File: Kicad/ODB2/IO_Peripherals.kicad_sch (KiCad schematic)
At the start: 22 parts, among them J5 RFM_Conn_Coaxial, U10 W25Q512JVEIQ

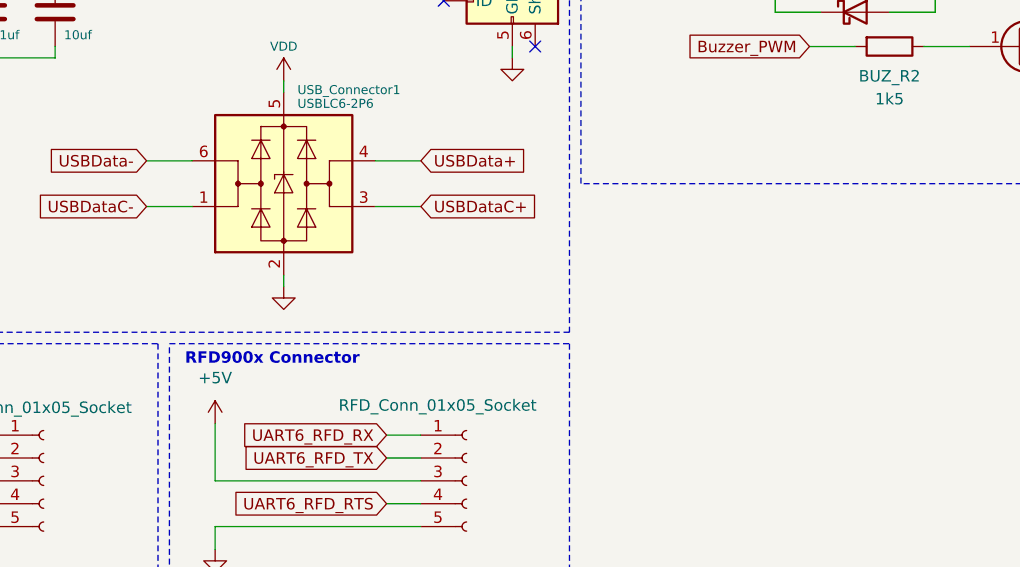
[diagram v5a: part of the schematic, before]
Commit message: ajout IO_Camera + stm32cubeide
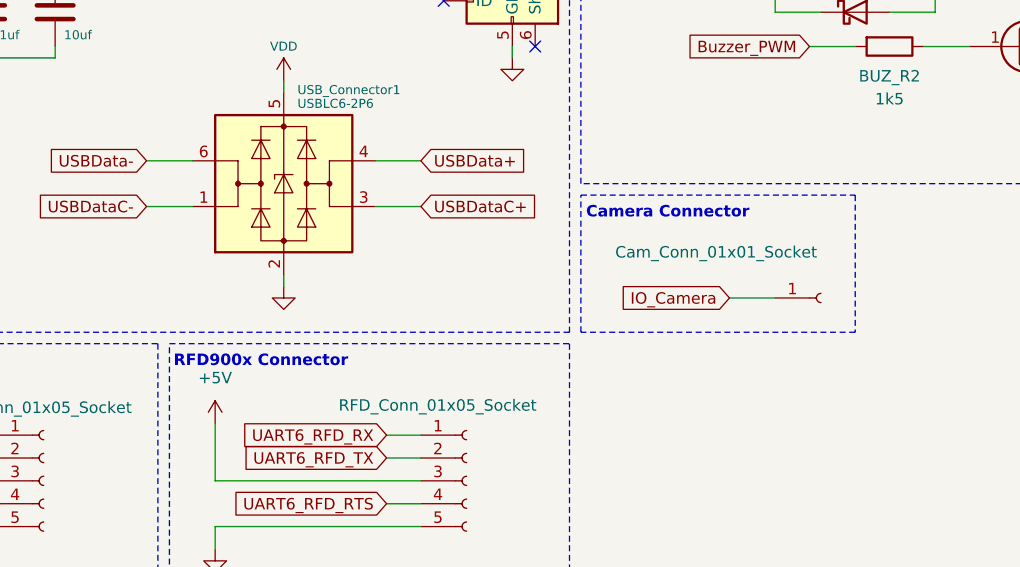
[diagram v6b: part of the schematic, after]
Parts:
- added J1: Cam_Conn_01x01_Socket, Connector_PinHeader_2.00mm:PinHeader_1x01_P2.00mm_Vertical, symbol Connector:Conn_01x01_Socket
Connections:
- new net IO_Camera: J1.1 (Pin_1)
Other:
- note added: "Camera Connector"
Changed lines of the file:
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@@
+	(wire
+		(pts
+			(xy 121.92 74.93) (xy 127 74.93)
+		)
+		(stroke
+			(width 0)
+			(type default)
+		)
+	)
 	(wire
 		(pts
@@
 			(width 0)
 			(type default)
+		)
+	)
+	(rectangle
+		(start 105.41 63.5)
+		(end 135.89 78.74)
+		(stroke
+			(width 0)
+			(type dash)
+		)
+		(fill
+			(type none)
 		)
 	)
@@
 		)
 	)
+	(text "Camera Connector"
+		(exclude_from_sim no)
+		(at 115.062 65.532 0)
+		(effects
+			(font
+				(size 1.27 1.27)
+				(thickness 0.254)
+				(bold yes)
+			)
+		)
+	)
 	(text "Standard SPI D0"
 		(exclude_from_sim no)
@@
 	(text "RFD900x Connector"
 		(exclude_from_sim no)
-		(at 71.12 81.788 0)
+		(at 69.85 82.042 0)
 		(effects
 			(font
@@
 		(property "Intersheetrefs" "${INTERSHEET_REFS}"
 			(at 116.3344 46.99 0)
+			(effects
+				(font
+					(size 1.27 1.27)
+				)
+				(justify right)
+				(hide yes)
+			)
+		)
+	)
+	(global_label "IO_Camera"
+		(shape input)
+		(at 121.92 74.93 180)
+		(fields_autoplaced yes)
+		(effects
+			(font
+				(size 1.27 1.27)
+			)
+			(justify right)
+		)
+		(property "Intersheetrefs" "${INTERSHEET_REFS}"
+			(at 108.8958 74.93 0)
 			(effects
 				(font
@@
 					(unit 1)
 				)
+			)
+		)
+	)
+	(symbol
+		(lib_id "Connector:Conn_01x01_Socket")
+		(at 132.08 74.93 0)
+		(unit 1)
+		(exclude_from_sim no)
+		(in_bom yes)
+		(on_board yes)
+		(dnp no)
+		(property "Reference" "J1"
+			(at 133.35 73.6599 0)
+			(effects
+				(font
+					(size 1.27 1.27)
+				)
+				(justify left)
+				(hide yes)
+			)
+		)
+		(property "Value" "Cam_Conn_01x01_Socket"
+			(at 109.22 69.85 0)
+			(effects
+				(font
+					(size 1.27 1.27)
+				)
+				(justify left)
+			)
+		)
+		(property "Footprint" "Connector_PinHeader_2.00mm:PinHeader_1x01_P2.00mm_Vertical"
+			(at 132.08 74.93 0)
+			(effects
+				(font
+					(size 1.27 1.27)
+				)
+				(hide yes)
+			)
+		)
+		(property "Datasheet" "~"
+			(at 132.08 74.93 0)
+			(effects
+				(font
+					(size 1.27 1.27)
+				)
+				(hide yes)
+			)
+		)
+		(property "Description" "Generic connector, single row, 01x01, script generated"
+			(at 132.08 74.93 0)
+			(effects
+				(font
+					(size 1.27 1.27)
+				)
+				(hide yes)
+			)
+		)
+		(pin "1"
+		)
+		(instances
+			(project ""
+				(path "/4b06c5d1-aa8b-48ed-8972-b43a60cfab78/93865dc8-71fa-4dc6-90ce-f5a9779dfd41"
+					(reference "J1")
+					(unit 1)
+				)

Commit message: fix my shit (cam io)
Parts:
- removed J1: Cam_Conn_01x01_Socket, Connector_PinHeader_2.00mm:PinHeader_1x01_P2.00mm_Vertical, symbol Connector:Conn_01x01_Socket
- added J1: Cam_Conn_01x02_Socket, Connector_PinHeader_2.00mm:PinHeader_1x02_P2.00mm_Vertical, symbol Connector:Conn_01x02_Socket
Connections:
- net GND: now also J1.2 (Pin_2)
- net IO_Camera: now also J1.1 (Pin_1)
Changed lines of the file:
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@@
 	(wire
 		(pts
+			(xy 124.46 76.2) (xy 123.19 76.2)
+		)
+		(stroke
+			(width 0)
+			(type default)
+		)
+	)
+	(wire
+		(pts
 			(xy 54.61 119.38) (xy 54.61 120.65)
 		)
@@
 	(wire
 		(pts
+			(xy 123.19 76.2) (xy 123.19 77.47)
+		)
+		(stroke
+			(width 0)
+			(type default)
+		)
+	)
+	(wire
+		(pts
 			(xy 64.77 95.25) (xy 87.63 95.25)
 		)
@@
 	(wire
 		(pts
-			(xy 121.92 74.93) (xy 127 74.93)
+			(xy 119.38 73.66) (xy 124.46 73.66)
 		)
 		(stroke
@@
 	(rectangle
 		(start 105.41 63.5)
-		(end 135.89 78.74)
+		(end 135.89 83.82)
 		(stroke
 			(width 0)
@@
 	(global_label "IO_Camera"
 		(shape input)
-		(at 121.92 74.93 180)
+		(at 119.38 73.66 180)
 		(fields_autoplaced yes)
 		(effects
@@
 		)
 		(property "Intersheetrefs" "${INTERSHEET_REFS}"
-			(at 108.8958 74.93 0)
+			(at 106.3558 73.66 0)
 			(effects
 				(font
@@
 	)
 	(symbol
-		(lib_id "Connector:Conn_01x01_Socket")
-		(at 132.08 74.93 0)
-		(unit 1)
-		(exclude_from_sim no)
-		(in_bom yes)
-		(on_board yes)
-		(dnp no)
-		(property "Reference" "J1"
-			(at 133.35 73.6599 0)
-			(effects
-				(font
-					(size 1.27 1.27)
-				)
-				(justify left)
-				(hide yes)
-			)
-		)
-		(property "Value" "Cam_Conn_01x01_Socket"
-			(at 109.22 69.85 0)
-			(effects
-				(font
-					(size 1.27 1.27)
-				)
-				(justify left)
-			)
-		)
-		(property "Footprint" "Connector_PinHeader_2.00mm:PinHeader_1x01_P2.00mm_Vertical"
-			(at 132.08 74.93 0)
-			(effects
-				(font
-					(size 1.27 1.27)
-				)
-				(hide yes)
-			)
-		)
-		(property "Datasheet" "~"
-			(at 132.08 74.93 0)
-			(effects
-				(font
-					(size 1.27 1.27)
-				)
-				(hide yes)
-			)
-		)
-		(property "Description" "Generic connector, single row, 01x01, script generated"
-			(at 132.08 74.93 0)
-			(effects
-				(font
-					(size 1.27 1.27)
-				)
-				(hide yes)
-			)
-		)
-		(pin "1"
-		)
-		(instances
-			(project ""
-				(path "/4b06c5d1-aa8b-48ed-8972-b43a60cfab78/93865dc8-71fa-4dc6-90ce-f5a9779dfd41"
-					(reference "J1")
-					(unit 1)
-				)
-			)
-		)
-	)
-	(symbol
 		(lib_id "Device:R")
 		(at 250.19 46.99 90)
@@
 	)
 	(symbol
+		(lib_id "power:GND")
+		(at 123.19 77.47 0)
+		(unit 1)
+		(exclude_from_sim no)
+		(in_bom yes)
+		(on_board yes)
+		(dnp no)
+		(fields_autoplaced yes)
+		(property "Reference" "#PWR082"
+			(at 123.19 83.82 0)
+			(effects
+				(font
+					(size 1 1)
+				)
+				(hide yes)
+			)
+		)
+		(property "Value" "GND"
+			(at 123.19 82.55 0)
+			(effects
+				(font
+					(size 1 1)
+				)
+				(hide yes)
+			)
+		)
+		(property "Footprint" ""
+			(at 123.19 77.47 0)
+			(effects
+				(font
+					(size 1 1)
+				)
+				(hide yes)
+			)
+		)
+		(property "Datasheet" ""
+			(at 123.19 77.47 0)
+			(effects
+				(font
+					(size 1 1)
+				)
+				(hide yes)
+			)
+		)
+		(property "Description" ""
+			(at 123.19 77.47 0)
+			(effects
+				(font
+					(size 1.27 1.27)
+				)
+				(hide yes)
+			)
+		)
+		(pin "1"
+		)
+		(instances
+			(project "ODB2"
+				(path "/4b06c5d1-aa8b-48ed-8972-b43a60cfab78/93865dc8-71fa-4dc6-90ce-f5a9779dfd41"
+					(reference "#PWR082")
+					(unit 1)
+				)
+			)
+		)
+	)
+	(symbol
 		(lib_id "Device:R")
 		(at 40.64 119.38 270)
@@
 					(unit 1)
 				)
+			)
+		)
+	)
+	(symbol
+		(lib_id "Connector:Conn_01x02_Socket")
+		(at 129.54 73.66 0)
+		(unit 1)
+		(exclude_from_sim no)
+		(in_bom yes)
+		(on_board yes)
+		(dnp no)
+		(property "Reference" "J1"
+			(at 130.81 73.6599 0)
+			(effects
+				(font
+					(size 1.27 1.27)
+				)
+				(justify left)
+				(hide yes)
+			)
+		)
+		(property "Value" "Cam_Conn_01x02_Socket"
+			(at 110.744 70.358 0)
+			(effects
+				(font
+					(size 1.27 1.27)
+				)
+				(justify left)
+			)
+		)
+		(property "Footprint" "Connector_PinHeader_2.00mm:PinHeader_1x02_P2.00mm_Vertical"
+			(at 129.54 73.66 0)
+			(effects
+				(font
+					(size 1.27 1.27)
+				)
+				(hide yes)
+			)
+		)
+		(property "Datasheet" "~"
+			(at 129.54 73.66 0)
+			(effects
+				(font
+					(size 1.27 1.27)
+				)
+				(hide yes)
+			)
+		)
+		(property "Description" "Generic connector, single row, 01x02, script generated"
+			(at 129.54 73.66 0)
+			(effects
+				(font
+					(size 1.27 1.27)
+				)
+				(hide yes)
+			)
+		)
+		(pin "1"
+		)
+		(pin "2"
+		)
+		(instances
+			(project ""
+				(path "/4b06c5d1-aa8b-48ed-8972-b43a60cfab78/93865dc8-71fa-4dc6-90ce-f5a9779dfd41"
+					(reference "J1")
+					(unit 1)
+				)

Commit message: ajout cam2
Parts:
- added J2: Cam2_Conn_01x02_Socket, Connector_PinHeader_2.00mm:PinHeader_1x02_P2.00mm_Vertical, symbol Connector:Conn_01x02_Socket
- J1: value Cam_Conn_01x02_Socket -> Cam1_Conn_01x02_Socket
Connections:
- net GND: now also J2.2 (Pin_2)
- net IO_Camera renamed IO_Camera1
- new net IO_Camera2: J2.1 (Pin_1)
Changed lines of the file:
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@@
 	(wire
 		(pts
+			(xy 120.65 85.09) (xy 125.73 85.09)
+		)
+		(stroke
+			(width 0)
+			(type default)
+		)
+	)
+	(wire
+		(pts
 			(xy 31.75 48.26) (xy 39.37 48.26)
 		)
@@
 	(wire
 		(pts
+			(xy 124.46 87.63) (xy 124.46 88.9)
+		)
+		(stroke
+			(width 0)
+			(type default)
+		)
+	)
+	(wire
+		(pts
+			(xy 125.73 87.63) (xy 124.46 87.63)
+		)
+		(stroke
+			(width 0)
+			(type default)
+		)
+	)
+	(wire
+		(pts
 			(xy 31.75 33.02) (xy 31.75 39.37)
 		)
@@
 	(wire
 		(pts
-			(xy 124.46 76.2) (xy 123.19 76.2)
+			(xy 125.73 76.2) (xy 124.46 76.2)
 		)
 		(stroke
@@
 	(wire
 		(pts
-			(xy 123.19 76.2) (xy 123.19 77.47)
+			(xy 124.46 76.2) (xy 124.46 77.47)
 		)
 		(stroke
@@
 	(wire
 		(pts
-			(xy 119.38 73.66) (xy 124.46 73.66)
+			(xy 120.65 73.66) (xy 125.73 73.66)
 		)
 		(stroke
@@
 	(rectangle
 		(start 105.41 63.5)
-		(end 135.89 83.82)
+		(end 135.89 100.33)
 		(stroke
 			(width 0)
@@
 		)
 	)
-	(global_label "IO_Camera"
+	(global_label "IO_Camera1"
 		(shape input)
-		(at 119.38 73.66 180)
+		(at 120.65 73.66 180)
 		(fields_autoplaced yes)
 		(effects
@@
 		)
 		(property "Intersheetrefs" "${INTERSHEET_REFS}"
-			(at 106.3558 73.66 0)
+			(at 106.4163 73.66 0)
 			(effects
 				(font
@@
 		)
 	)
+	(global_label "IO_Camera2"
+		(shape input)
+		(at 120.65 85.09 180)
+		(fields_autoplaced yes)
+		(effects
+			(font
+				(size 1.27 1.27)
+			)
+			(justify right)
+		)
+		(property "Intersheetrefs" "${INTERSHEET_REFS}"
+			(at 106.4163 85.09 0)
+			(effects
+				(font
+					(size 1.27 1.27)
+				)
+				(justify right)
+				(hide yes)
+			)
+		)
+	)
 	(global_label "SYS_SWCLK"
 		(shape input)
@@
 	(symbol
 		(lib_id "power:GND")
-		(at 123.19 77.47 0)
+		(at 124.46 77.47 0)
 		(unit 1)
 		(exclude_from_sim no)
@@
 		(fields_autoplaced yes)
 		(property "Reference" "#PWR082"
-			(at 123.19 83.82 0)
+			(at 124.46 83.82 0)
 			(effects
 				(font
@@
 		)
 		(property "Value" "GND"
-			(at 123.19 82.55 0)
+			(at 124.46 82.55 0)
 			(effects
 				(font
@@
 		)
 		(property "Footprint" ""
-			(at 123.19 77.47 0)
+			(at 124.46 77.47 0)
 			(effects
 				(font
@@
 		)
 		(property "Datasheet" ""
-			(at 123.19 77.47 0)
+			(at 124.46 77.47 0)
 			(effects
 				(font
@@
 		)
 		(property "Description" ""
-			(at 123.19 77.47 0)
+			(at 124.46 77.47 0)
 			(effects
 				(font
@@
 	)
 	(symbol
+		(lib_id "Connector:Conn_01x02_Socket")
+		(at 130.81 85.09 0)
+		(unit 1)
+		(exclude_from_sim no)
+		(in_bom yes)
+		(on_board yes)
+		(dnp no)
+		(property "Reference" "J2"
+			(at 132.08 85.0899 0)
+			(effects
+				(font
+					(size 1.27 1.27)
+				)
+				(justify left)
+				(hide yes)
+			)
+		)
+		(property "Value" "Cam2_Conn_01x02_Socket"
+			(at 107.95 81.788 0)
+			(effects
+				(font
+					(size 1.27 1.27)
+				)
+				(justify left)
+			)
+		)
+		(property "Footprint" "Connector_PinHeader_2.00mm:PinHeader_1x02_P2.00mm_Vertical"
+			(at 130.81 85.09 0)
+			(effects
+				(font
+					(size 1.27 1.27)
+				)
+				(hide yes)
+			)
+		)
+		(property "Datasheet" "~"
+			(at 130.81 85.09 0)
+			(effects
+				(font
+					(size 1.27 1.27)
+				)
+				(hide yes)
+			)
+		)
+		(property "Description" "Generic connector, single row, 01x02, script generated"
+			(at 130.81 85.09 0)
+			(effects
+				(font
+					(size 1.27 1.27)
+				)
+				(hide yes)
+			)
+		)
+		(pin "1"
+		)
+		(pin "2"
+		)
+		(instances
+			(project "ODB2"
+				(path "/4b06c5d1-aa8b-48ed-8972-b43a60cfab78/93865dc8-71fa-4dc6-90ce-f5a9779dfd41"
+					(reference "J2")
+					(unit 1)
+				)
+			)
+		)
+	)
+	(symbol
 		(lib_id "power:GND")
 		(at 223.52 99.06 0)
@@
 	)
 	(symbol
+		(lib_id "power:GND")
+		(at 124.46 88.9 0)
+		(unit 1)
+		(exclude_from_sim no)
+		(in_bom yes)
+		(on_board yes)
+		(dnp no)
+		(fields_autoplaced yes)
+		(property "Reference" "#PWR093"
+			(at 124.46 95.25 0)
+			(effects
+				(font
+					(size 1 1)
+				)
+				(hide yes)
+			)
+		)
+		(property "Value" "GND"
+			(at 124.46 93.98 0)
+			(effects
+				(font
+					(size 1 1)
+				)
+				(hide yes)
+			)
+		)
+		(property "Footprint" ""
+			(at 124.46 88.9 0)
+			(effects
+				(font
+					(size 1 1)
+				)
+				(hide yes)
+			)
+		)
+		(property "Datasheet" ""
+			(at 124.46 88.9 0)
+			(effects
+				(font
+					(size 1 1)
+				)
+				(hide yes)
+			)
+		)
+		(property "Description" ""
+			(at 124.46 88.9 0)
+			(effects
+				(font
+					(size 1.27 1.27)
+				)
+				(hide yes)
+			)
+		)
+		(pin "1"
+		)
+		(instances
+			(project "ODB2"
+				(path "/4b06c5d1-aa8b-48ed-8972-b43a60cfab78/93865dc8-71fa-4dc6-90ce-f5a9779dfd41"
+					(reference "#PWR093")
+					(unit 1)
+				)
+			)
+		)
+	)
+	(symbol
 		(lib_id "Connector:Conn_01x05_Socket")
 		(at 45.72 95.25 0)
@@
 	(symbol
 		(lib_id "Connector:Conn_01x02_Socket")
-		(at 129.54 73.66 0)
+		(at 130.81 73.66 0)
 		(unit 1)
 		(exclude_from_sim no)
@@
 		(dnp no)
 		(property "Reference" "J1"
-			(at 130.81 73.6599 0)
+			(at 132.08 73.6599 0)
 			(effects
 				(font
@@
 			)
 		)
-		(property "Value" "Cam_Conn_01x02_Socket"
-			(at 110.744 70.358 0)
+		(property "Value" "Cam1_Conn_01x02_Socket"
+			(at 107.95 70.358 0)
 			(effects
 				(font
@@
 		)
 		(property "Footprint" "Connector_PinHeader_2.00mm:PinHeader_1x02_P2.00mm_Vertical"
-			(at 129.54 73.66 0)
+			(at 130.81 73.66 0)
 			(effects
 				(font
@@
 		)
 		(property "Datasheet" "~"
-			(at 129.54 73.66 0)
+			(at 130.81 73.66 0)
 			(effects
 				(font
@@
 		)
 		(property "Description" "Generic connector, single row, 01x02, script generated"
-			(at 129.54 73.66 0)
+			(at 130.81 73.66 0)
 			(effects
 				(font
